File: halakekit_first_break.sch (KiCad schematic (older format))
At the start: 29 parts, among them J1 HEADER_3, J10 HEADER_3, J11 HEADER_3, J12 HEADER_3, J13 HEADER_3, J14 HEADER_3, J15 HEADER_3, J16 HEADER_3, J17 HEADER_3, J18 HEADER_3, J19 HEADER_3, J2 HEADER_3, J20 HEADER_3, J21 HEADER_10, J22 HEADER_10, J23 HEADER_2x2, J24 HEADER_4, J25 HEADER_12, J26 HEADER_2, J27 HEADER_12, J28 HEADER_4, J3 HEADER_3, J4 HEADER_3, J5 HEADER_3, J6 HEADER_3, J7 HEADER_3, J8 HEADER_3, J9 HEADER_3, U1 Arduino_Pro_Micro

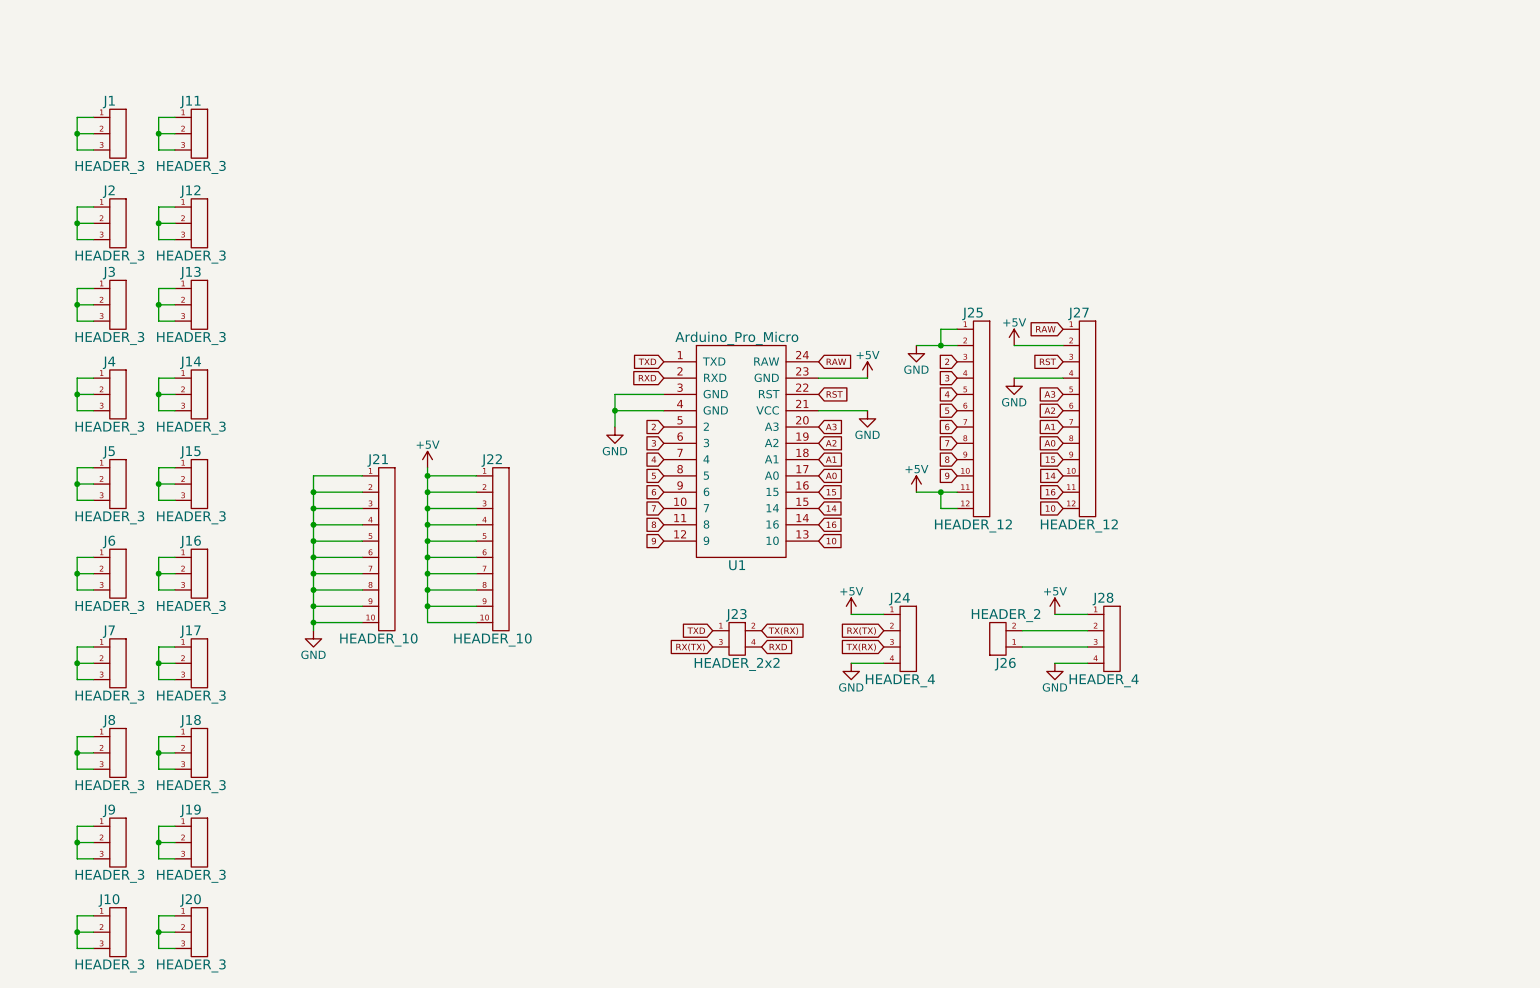
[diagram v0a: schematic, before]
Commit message: Update schema for rev1.1
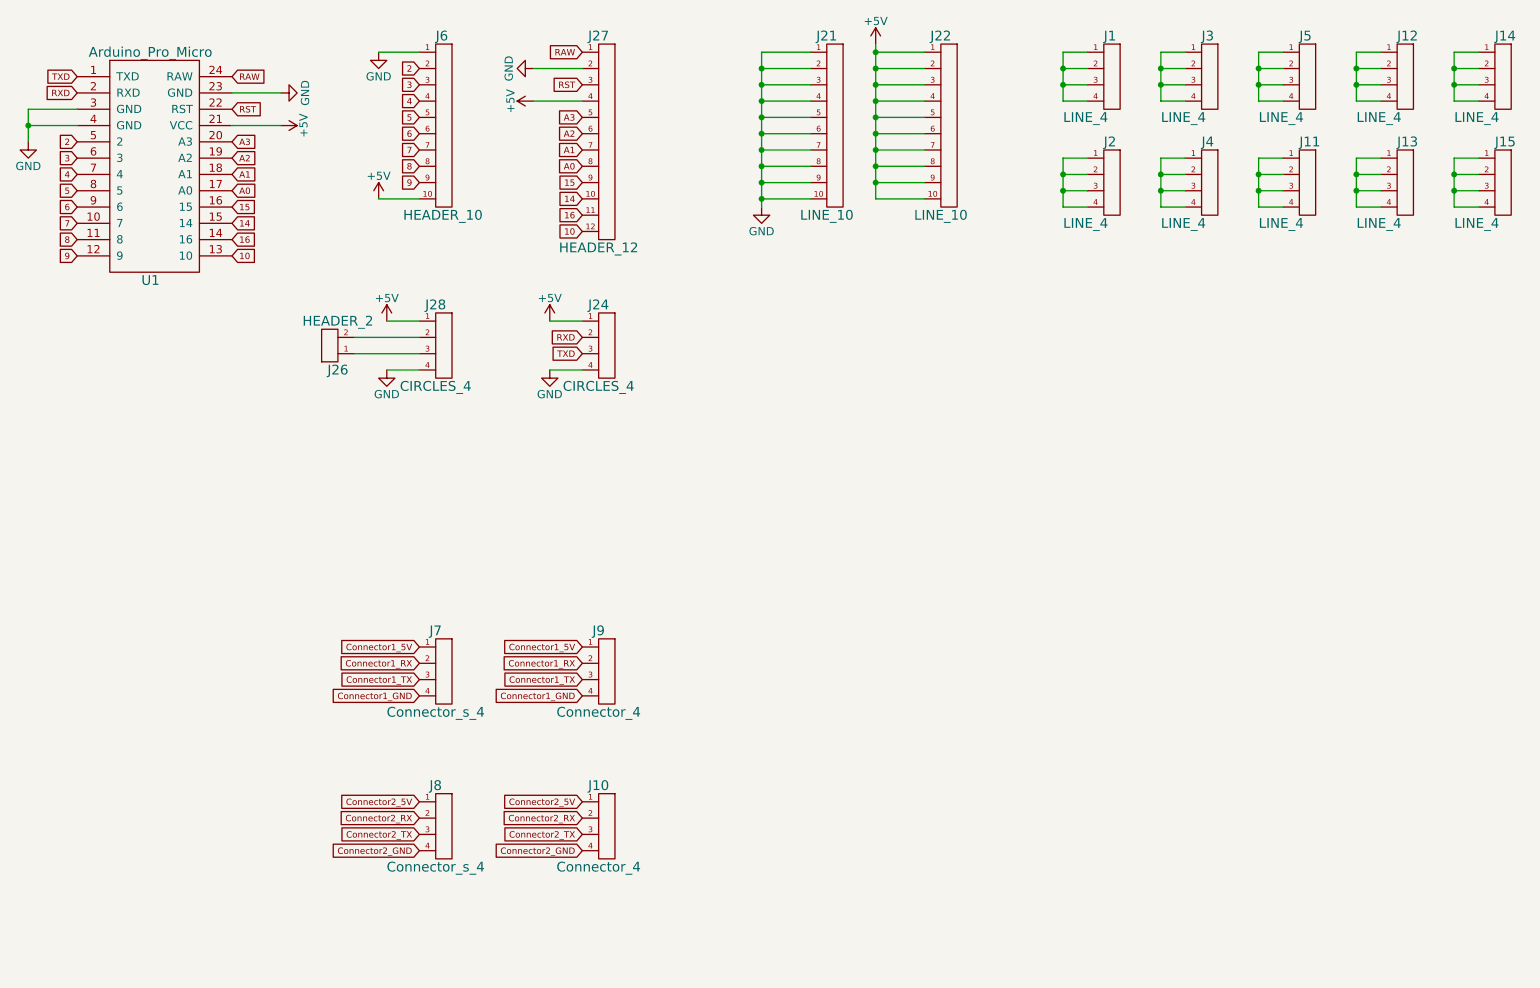
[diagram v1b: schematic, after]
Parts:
- removed J1, J10, J11, J12, J13, J14, J15, J16, J17, J18, J19, J2, J20, J3, J4, J5, J6, J7, J8, J9: HEADER_3, simple_headers:Pin_Header_Straight_1x03, symbol HEADER_3
- removed J23: HEADER_2x2, simple_headers:Pin_Header_Straight_2x02, symbol HEADER_2x2
- removed J25: HEADER_12, simple_headers:Pin_Header_Straight_1x12, symbol HEADER_12
- added J1, J11, J12, J13, J14, J15, J2, J3, J4, J5: LINE_4, simple_headers:Pin_Header_Connect_1x04, symbol HEADER_4
- added J10, J9: Connector_4, simple_headers:Pin_Header_Straight_1x04, symbol HEADER_4
- added J6: HEADER_10, simple_headers:Pin_Header_Straight_1x10, symbol HEADER_10
- added J7, J8: Connector_s_4, simple_headers:headers_s_4, symbol HEADER_4
- J21, J22: value HEADER_10 -> LINE_10
- J24, J28: value HEADER_4 -> CIRCLES_4; footprint simple_headers:Pin_Header_Straight_1x04 -> simple_headers:Pin_Header_Circle_1x04
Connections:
- net RX(TX) is gone; now on net RXD: J24.2
- net TX(RX) is gone; now on net TXD: J24.3
- net +5V: now also J27.4, U1.21 (VCC), J6.10; no longer J27.2, U1.23 (GND)
- net 2: now also J6.2
- net 3: now also J6.3
- net 4: now also J6.4
- net 5: now also J6.5
- net 6: now also J6.6
- net 7: now also J6.7
- net 8: now also J6.8
- net 9: now also J6.9
- net GND: now also J27.2, U1.23 (GND), J6.1; no longer J27.4, U1.21 (VCC)
- new net: J1.1, J1.2, J1.3, J1.4
- new net: J2.1, J2.2, J2.3, J2.4
- new net: J3.1, J3.2, J3.3, J3.4
- new net: J4.1, J4.2, J4.3, J4.4
- new net: J5.1, J5.2, J5.3, J5.4
- new net: J11.1, J11.2, J11.3, J11.4
- new net: J12.1, J12.2, J12.3, J12.4
- new net: J13.1, J13.2, J13.3, J13.4
- new net: J14.1, J14.2, J14.3, J14.4
- new net: J15.1, J15.2, J15.3, J15.4
- new net Connector1_5V: J7.1, J9.1
- new net Connector1_GND: J7.4, J9.4
- new net Connector1_RX: J7.2, J9.2
- new net Connector1_TX: J7.3, J9.3
- new net Connector2_5V: J10.1, J8.1
- new net Connector2_GND: J10.4, J8.4
- new net Connector2_RX: J10.2, J8.2
- new net Connector2_TX: J10.3, J8.3
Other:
- moved on the sheet: J21, J22, J24, J26, J27, J28, U1

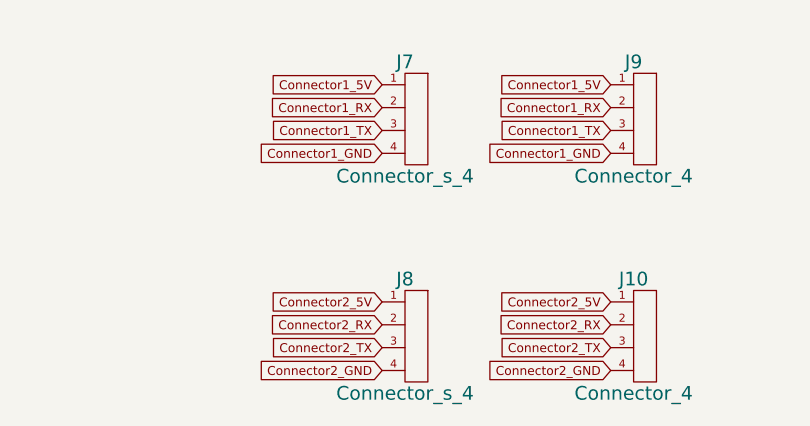
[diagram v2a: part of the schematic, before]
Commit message: Change size of holl and connector footprint larger
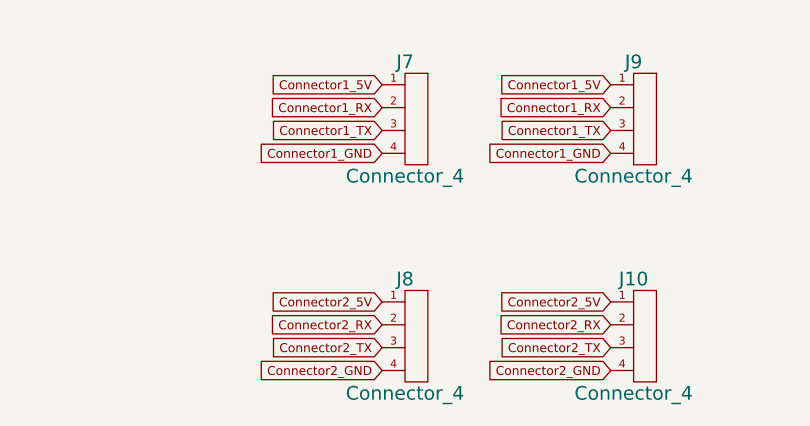
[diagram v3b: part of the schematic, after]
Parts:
- J7, J8: value Connector_s_4 -> Connector_4; footprint simple_headers:headers_s_4 -> simple_headers:Pin_Header_Straight_1x04
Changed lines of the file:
@@
 LIBS:w_connectors
 LIBS:halakekit_first_break-cache
-EELAYER 26 0
+EELAYER 25 0
 EELAYER END
 $Descr A4 11693 8268
@@
 P 3900 5250
 F 0 "J7" H 3900 5500 60  0000 C CNN
-F 1 "Connector_s_4" H 3900 5000 60  0000 C CNN
-F 2 "simple_headers:headers_s_4" H 3900 5250 60  0001 C CNN
+F 1 "Connector_4" H 3900 5000 60  0000 C CNN
+F 2 "simple_headers:Pin_Header_Straight_1x04" H 3900 5250 60  0001 C CNN
 F 3 "" H 3900 5250 60  0000 C CNN
 	1    3900 5250
@@
 P 3900 6200
 F 0 "J8" H 3900 6450 60  0000 C CNN
-F 1 "Connector_s_4" H 3900 5950 60  0000 C CNN
-F 2 "simple_headers:headers_s_4" H 3900 6200 60  0001 C CNN
+F 1 "Connector_4" H 3900 5950 60  0000 C CNN
+F 2 "simple_headers:Pin_Header_Straight_1x04" H 3900 6200 60  0001 C CNN
 F 3 "" H 3900 6200 60  0000 C CNN
 	1    3900 6200
